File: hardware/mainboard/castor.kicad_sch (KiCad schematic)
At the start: 46 parts, among them J7 OSC OUT, Q1 MMBT3906, U10 MCP6001-OT, U7 TL074, U8 TL074, U9 74LVC2G74

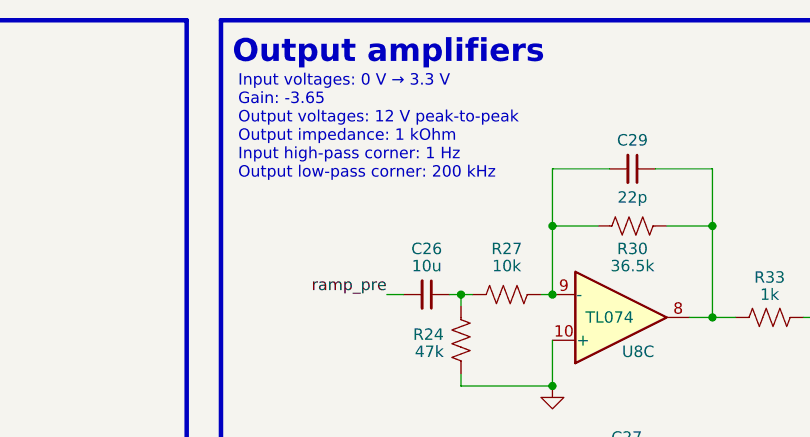
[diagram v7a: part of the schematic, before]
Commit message: Switch audio filter caps to 0603. Start auditing BOM
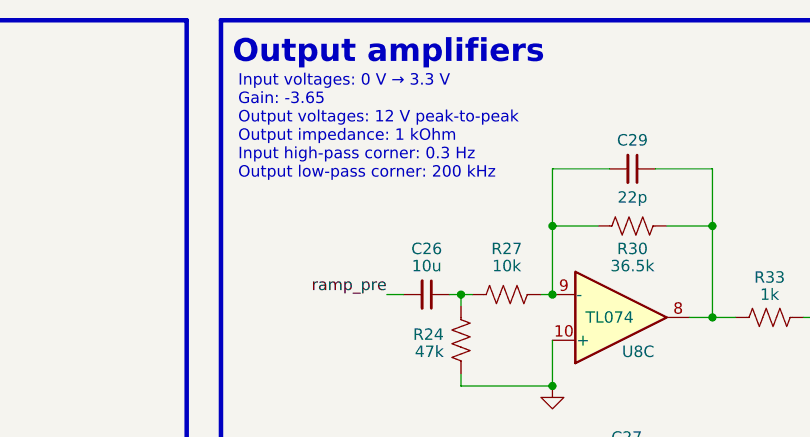
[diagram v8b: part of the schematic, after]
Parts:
- C22: Reqs C0G 1%, 6v+, ramp core -> Ramp core, C0G 1% or better, 6 V; finalized yes -> (none); mpn VJ0603A271FXAPW1BC -> (none); mpn specs 1%, 50v -> (none)
- C23: Reqs C0G 1%+, 6v+, ramp core -> Ramp core, C0G 1% or better, 6 V; finalized yes & alt -> (none); mpn GRM1885C1H102FA01J -> (none); mpn alt GRM1885C1H102FA01* -> (none); mpn specs 1%, 50v -> (none)
- C24: footprint Capacitor_SMD:C_0805_2012Metric_Pad1.18x1.45mm_HandSolder -> Capacitor_SMD:C_0603_1608Metric_Pad1.08x0.95mm_HandSolder; Reqs audio path, low-voltage (3.3V), 16V -> Low voltage audio, 10 V; finalized yes & alt -> (none); mpn (none) -> CL10A106MP8NNNC
- C25: footprint Capacitor_SMD:C_0805_2012Metric_Pad1.18x1.45mm_HandSolder -> Capacitor_SMD:C_0603_1608Metric_Pad1.08x0.95mm_HandSolder; Reqs audio path, low-voltage (3.3V), 16V -> Low voltage audio, 10 V; finalized no -> (none); mpn (none) -> CL10A106MP8NNNC
- C26: footprint Capacitor_SMD:C_0805_2012Metric_Pad1.18x1.45mm_HandSolder -> Capacitor_SMD:C_0603_1608Metric_Pad1.08x0.95mm_HandSolder; Reqs audio path, low-voltage (3.3V), 16V -> Low voltage audio, 10 V; mpn (none) -> CL10A106MP8NNNC
- C27, C28, C29: Reqs audio filter, 20v+ -> Eurorack level audio filter, 16 V; finalized yes -> (none); mpn MF-CAP-0603-22pF -> (none); mpn alt GCM1885C2A220JA16J -> (none); mpn specs 5% 50v -> (none)
- C30: Reqs audio filter, 20v+ -> Eurorack level audio filter, 16 V; finalized yes -> (none); mpn VJ0603A8R2DXACW1BC -> (none); mpn alt GRM1885C1H8R2WA01D -> (none); mpn specs 25v -> (none)
- C46, C47, C48, C49: Reqs bypass, 16v+ -> Bypass, 16 V; finalized yes -> (none); mpn MF-CAP-0603-0.1uF -> (none); mpn alt GCM188R91E104KA37D -> (none); mpn specs 10%, 25v -> (none)
- J7: finalized (none) -> yes
- Q1: finalized yes -> (none); macrofab_mpn (none) -> MF-DSC-SOT233-MMBT3906; mpn MF-DSC-SOT233-MMBT3906 -> MMBT3906L; mpn alt MMBT3906L -> (none)
- R16: Reqs 1%, 15mW, control path -> Digital control path, 1%, 15 mW; finalized yes -> (none); mpn RG1608P-103-D-T5 -> (none); mpn alt RR0816P-103-D -> (none); mpn alts 2 ERA-3AED103V -> (none); mpn specs 62mW, 0.5% -> (none)
- R17: Reqs 5%, 1mW, control path -> Analog control path, 0.5%, 1 mW; finalized yes -> (none); mpn RR0816P-204-D -> (none); mpn alt ERA-3AEB204V -> (none); mpn specs 62mW, 0.5% -> (none)
- R18: Reqs 5%, 12mW, control path -> Digital control path, 5%, 12 mW; finalized yes -> (none); mpn MCT06030C1001FP500 -> (none); mpn alt ERA-3AEB102V -> (none); mpn specs 100mW, 1% -> (none)
- R19: Reqs 1%, >50mW, audio path -> Ramp core, 1%, 50 mW; finalized yes -> (none); mpn MCT06030C2700FP500 -> (none); mpn specs 100mW, 1% -> (none)
- R20: Reqs 1%, 5mW, audio path -> Low voltage audio, 1%, 5 mW; finalized yes -> (none); mpn RR0816P-303-D -> (none); mpn alt ERA-3AEB303V -> (none); mpn specs 62mW, 0.5% -> (none)
- R21, R25, R26, R27: Reqs 1%, 15mW, audio path -> Low voltage audio, 1%, 15 mW; finalized yes -> (none); mpn RG1608P-103-D-T5 -> (none); mpn alt RR0816P-103-D -> (none); mpn alts 2 ERA-3AED103V -> (none); mpn specs 62mW, 0.5% -> (none)
- R22, R23, R24: Reqs 1%, 4mW, audio path -> Low voltage audio, 1%, 15 mW; finalized yes -> (none); mpn RR0816P-473-D -> (none); mpn alt ERA-3AED473V -> (none); mpn alts 2 RT0603DRD0747KL -> (none); mpn specs 62mW, 0.5% -> (none)
- R28, R29, R30: Reqs 1%, 5mW, audio path -> Eurorack level audio, 1%, 5 mW; finalized yes -> (none); mpn RR0816P-3652-D-55C -> (none); mpn alt ERA-3AEB3652V -> (none); mpn specs 62mW, 0.5% -> (none)
- R31, R32, R33, R38: Reqs 5%, 150mW, audio output -> Output impedance, 5%, 150 mW; finalized yes -> (none); mpn MCT06030C1001FP500 -> MCT06030C1001FP500, ERA-3AEB102V; mpn alt ERA-3AEB102V -> (none); mpn specs 100mW, 1% -> (none)
- R34, R35, R36, R37: Reqs 1%, 2mW, audio path -> Eurorack level audio, 1%, 2 mW; finalized yes -> (none); mpn RR0816P-104-D -> (none); mpn alt ERA-3AED104V -> (none); mpn specs 62mW, 0.5% -> (none)
- TP11: finalized yes -> n/a
- U10: finalized yes -> (none); mpn MCP6001T-I/OT -> MCP6001T-I/OT, AD8541ARTZ; mpn alt AD8541ARTZ -> (none)
- U9: finalized yes -> (none)
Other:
- note added: "Input voltages: 0 V → 3.3 V Gain: -3.65 Output voltages: 12 V peak-to-peak Output impedance: 1 kOhm Input high-pass corner: 0.3 Hz Output low-pass corner: 200 kHz"
- note removed: "Input voltages: 0 V → 3.3 V Gain: -3.65 Output voltages: 12 V peak-to-peak Output impedance: 1 kOhm Input high-pass corner: 1 Hz Output low-pass corner: 200 kHz"
